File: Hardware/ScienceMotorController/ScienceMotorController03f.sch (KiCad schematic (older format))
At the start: 16 parts

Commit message: changed everything to actuation, added schottky diode, added A/B flags to tiva
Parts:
- added FB?: Ferrite_Bead_Small, symbol Device:Ferrite_Bead_Small
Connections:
- net labels added: +12VA, +3.3VA
- net labels removed: +12V, +3.3V
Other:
- note added: "Sheet 03f: Mixer Output"
- note removed: "Sheet 03f: Motor Driver 6"
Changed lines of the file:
@@
 	7300 4200 7300 4100
 Connection ~ 7300 4100
-$Comp
-L power:+12V #PWR?
-U 1 1 5FACB535
-P 7500 3950
-AR Path="/5F7D111E/5FACB535" Ref="#PWR?"  Part="1"
-AR Path="/5F7D111E/5FA66A7C/5FACB535" Ref="#PWR?"  Part="1"
-F 0 "#PWR?" H 7500 3800 50  0001 C CNN
-F 1 "+12V" H 7515 4123 50  0000 C CNN
-F 2 "" H 7500 3950 50  0001 C CNN
-F 3 "" H 7500 3950 50  0001 C CNN
-	1    7500 3950
-	1    0    0    -1
-$EndComp
 Wire Wire Line
 	7500 3950 7500 4000
@@
 Wire Wire Line
 	5300 4150 5150 4150
-$Comp
-L power:+3.3V #PWR?
-U 1 1 5FACB576
-P 5150 4150
-AR Path="/5F7D111E/5FACB576" Ref="#PWR?"  Part="1"
-AR Path="/5F7D111E/5FA66A7C/5FACB576" Ref="#PWR?"  Part="1"
-F 0 "#PWR?" H 5150 4000 50  0001 C CNN
-F 1 "+3.3V" V 5165 4278 50  0000 L CNN
-F 2 "" H 5150 4150 50  0001 C CNN
-F 3 "" H 5150 4150 50  0001 C CNN
-	1    5150 4150
-	0    -1   -1   0
-$EndComp
-$Comp
-L power:+3.3V #PWR?
-U 1 1 5FACB57C
-P 5150 3850
-AR Path="/5F7D111E/5FACB57C" Ref="#PWR?"  Part="1"
-AR Path="/5F7D111E/5FA66A7C/5FACB57C" Ref="#PWR?"  Part="1"
-F 0 "#PWR?" H 5150 3700 50  0001 C CNN
-F 1 "+3.3V" V 5165 3978 50  0000 L CNN
-F 2 "" H 5150 3850 50  0001 C CNN
-F 3 "" H 5150 3850 50  0001 C CNN
-	1    5150 3850
-	0    -1   -1   0
-$EndComp
 Wire Wire Line
 	5650 3850 5150 3850
@@
 Wire Wire Line
 	5650 3750 5500 3750
-$Comp
-L power:+3.3V #PWR?
-U 1 1 5FACB58A
-P 5150 3750
-AR Path="/5F7D111E/5FACB58A" Ref="#PWR?"  Part="1"
-AR Path="/5F7D111E/5FA66A7C/5FACB58A" Ref="#PWR?"  Part="1"
-F 0 "#PWR?" H 5150 3600 50  0001 C CNN
-F 1 "+3.3V" V 5165 3878 50  0000 L CNN
-F 2 "" H 5150 3750 50  0001 C CNN
-F 3 "" H 5150 3750 50  0001 C CNN
-	1    5150 3750
-	0    -1   -1   0
-$EndComp
 Wire Wire Line
 	5300 3750 5150 3750
@@
 	8100 3600 8200 3600
 Text Notes 7200 6950 0    197  ~ 0
-Sheet 03f: Motor Driver 6
+Sheet 03f: Mixer Output
+$Comp
+L Device:Ferrite_Bead_Small FB?
+U 1 1 5F83E921
+P 8450 4150
+F 0 "FB?" H 8550 4196 50  0000 L CNN
+F 1 "Ferrite_Bead_Small" H 8550 4105 50  0000 L CNN
+F 2 "" V 8380 4150 50  0001 C CNN
+F 3 "~" H 8450 4150 50  0001 C CNN
+	1    8450 4150
+	1    0    0    -1
+$EndComp
+$Comp
+L power:+3.3VA #PWR?
+U 1 1 5F83FF6A
+P 5150 3750
+F 0 "#PWR?" H 5150 3600 50  0001 C CNN
+F 1 "+3.3VA" V 5165 3877 50  0000 L CNN
+F 2 "" H 5150 3750 50  0001 C CNN
+F 3 "" H 5150 3750 50  0001 C CNN
+	1    5150 3750
+	0    -1   -1   0
+$EndComp
+$Comp
+L power:+3.3VA #PWR?
+U 1 1 5F8408BA
+P 5150 3850
+F 0 "#PWR?" H 5150 3700 50  0001 C CNN
+F 1 "+3.3VA" V 5165 3977 50  0000 L CNN
+F 2 "" H 5150 3850 50  0001 C CNN
+F 3 "" H 5150 3850 50  0001 C CNN
+	1    5150 3850
+	0    -1   -1   0
+$EndComp
+$Comp
+L power:+3.3VA #PWR?
+U 1 1 5F840B1F
+P 5150 4150
+F 0 "#PWR?" H 5150 4000 50  0001 C CNN
+F 1 "+3.3VA" V 5165 4277 50  0000 L CNN
+F 2 "" H 5150 4150 50  0001 C CNN
+F 3 "" H 5150 4150 50  0001 C CNN
+	1    5150 4150
+	0    -1   -1   0
+$EndComp
+$Comp
+L power:+12VA #PWR?
+U 1 1 5F8410BA
+P 7500 3950
+F 0 "#PWR?" H 7500 3800 50  0001 C CNN
+F 1 "+12VA" H 7515 4123 50  0000 C CNN
+F 2 "" H 7500 3950 50  0001 C CNN
+F 3 "" H 7500 3950 50  0001 C CNN
+	1    7500 3950
+	1    0    0    -1
+$EndComp
 $EndSCHEMATC

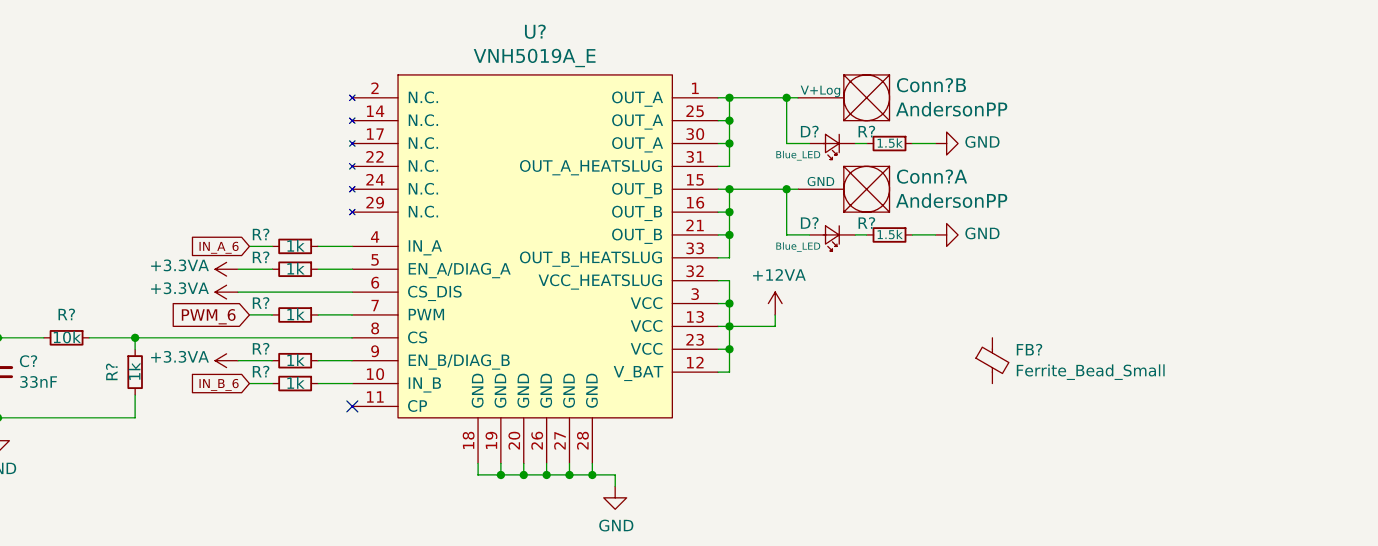
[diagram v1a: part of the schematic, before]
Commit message: added ferrite beads
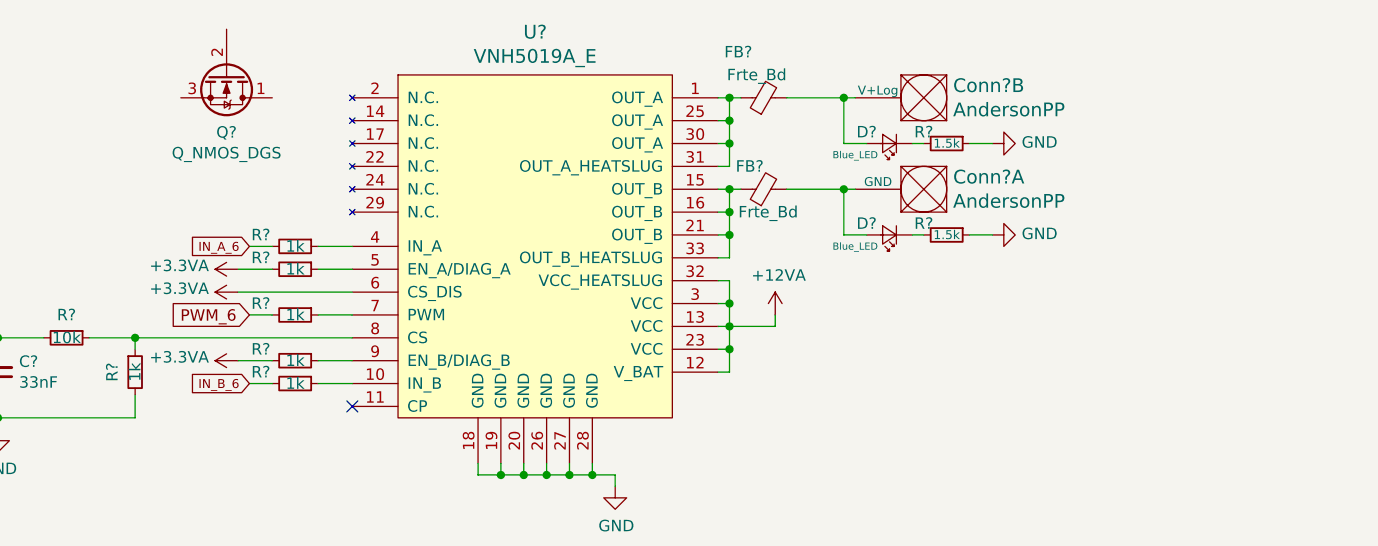
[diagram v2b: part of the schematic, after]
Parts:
- added FB?: Frte_Bd, symbol Device:Ferrite_Bead_Small
- added Q?: Q_NMOS_DGS, symbol Device:Q_NMOS_DGS
- FB?: value Ferrite_Bead_Small -> Frte_Bd
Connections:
- net at FB?.1: now also U?.15 (OUT_B), U?.16 (OUT_B), U?.21 (OUT_B), U?.33 (OUT_B_HEATSLUG)
- net at FB?.2: now also Conn?.1 (GND), D?.2 (A)
- net at U?.1 (OUT_A), U?.25 (OUT_A), U?.30 (OUT_A)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: now also FB?.1; no longer Conn?.2 (V+Log), D?.2 (A)
- new net: Conn?.2 (V+Log), D?.2 (A), FB?.2
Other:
- moved on the sheet: Conn?A, Conn?B, D?, FB?, R?
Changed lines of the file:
@@
 L MRDT_Connectors:AndersonPP Conn?
 U 1 1 5FACB5D5
-P 8000 3300
+P 8250 3300
 AR Path="/5F7D111E/5FACB5D5" Ref="Conn?"  Part="1"
 AR Path="/5F7D111E/5FA66A7C/5FACB5D5" Ref="Conn?"  Part="1"
-F 0 "Conn?" H 7972 3347 60  0000 R CNN
-F 1 "AndersonPP" H 7972 3453 60  0000 R CNN
-F 2 "" H 7850 2750 60  0001 C CNN
-F 3 "" H 7850 2750 60  0001 C CNN
-	1    8000 3300
+F 0 "Conn?" H 8222 3347 60  0000 R CNN
+F 1 "AndersonPP" H 8222 3453 60  0000 R CNN
+F 2 "" H 8100 2750 60  0001 C CNN
+F 3 "" H 8100 2750 60  0001 C CNN
+	1    8250 3300
 	-1   0    0    1
 $EndComp
@@
 L MRDT_Connectors:AndersonPP Conn?
 U 2 1 5FACB5DB
-P 8000 2900
+P 8250 2900
 AR Path="/5F7D111E/5FACB5DB" Ref="Conn?"  Part="2"
 AR Path="/5F7D111E/5FA66A7C/5FACB5DB" Ref="Conn?"  Part="2"
-F 0 "Conn?" H 7972 2947 60  0000 R CNN
-F 1 "AndersonPP" H 7972 3053 60  0000 R CNN
-F 2 "" H 7850 2350 60  0001 C CNN
-F 3 "" H 7850 2350 60  0001 C CNN
-	2    8000 2900
+F 0 "Conn?" H 8222 2947 60  0000 R CNN
+F 1 "AndersonPP" H 8222 3053 60  0000 R CNN
+F 2 "" H 8100 2350 60  0001 C CNN
+F 3 "" H 8100 2350 60  0001 C CNN
+	2    8250 2900
 	-1   0    0    1
 $EndComp
@@
 Connection ~ 4700 4050
 Wire Wire Line
-	7300 3000 7550 3000
-Connection ~ 7300 3000
-Wire Wire Line
-	7300 3400 7550 3400
-Connection ~ 7300 3400
-Wire Wire Line
-	7550 3200 7550 3000
-Connection ~ 7550 3000
-Wire Wire Line
-	7550 3000 7600 3000
-Wire Wire Line
-	7550 3200 7650 3200
-Wire Wire Line
-	7550 3400 7550 3600
-Wire Wire Line
-	7550 3600 7650 3600
-Connection ~ 7550 3400
-Wire Wire Line
-	7550 3400 7600 3400
+	7550 3000 7800 3000
+Wire Wire Line
+	7550 3400 7800 3400
+Wire Wire Line
+	7800 3200 7800 3000
+Connection ~ 7800 3000
+Wire Wire Line
+	7800 3000 7850 3000
+Wire Wire Line
+	7800 3200 7900 3200
+Wire Wire Line
+	7800 3400 7800 3600
+Wire Wire Line
+	7800 3600 7900 3600
+Connection ~ 7800 3400
+Wire Wire Line
+	7800 3400 7850 3400
 $Comp
 L Device:LED_Small D?
 U 1 1 5FACB5EF
-P 7750 3200
+P 8000 3200
 AR Path="/5F7D111E/5FACB5EF" Ref="D?"  Part="1"
 AR Path="/5F7D111E/5FA66A7C/5FACB5EF" Ref="D?"  Part="1"
-F 0 "D?" H 7850 3150 50  0000 C CNN
-F 1 "Blue_LED" H 7900 3250 31  0000 C CNN
-F 2 "" V 7750 3200 50  0001 C CNN
-F 3 "~" V 7750 3200 50  0001 C CNN
-	1    7750 3200
+F 0 "D?" H 8100 3150 50  0000 C CNN
+F 1 "Blue_LED" H 8150 3250 31  0000 C CNN
+F 2 "" V 8000 3200 50  0001 C CNN
+F 3 "~" V 8000 3200 50  0001 C CNN
+	1    8000 3200
 	-1   0    0    1
 $EndComp
@@
 L Device:LED_Small D?
 U 1 1 5FACB5F5
-P 7750 3600
+P 8000 3600
 AR Path="/5F7D111E/5FACB5F5" Ref="D?"  Part="1"
 AR Path="/5F7D111E/5FA66A7C/5FACB5F5" Ref="D?"  Part="1"
-F 0 "D?" H 7850 3550 50  0000 C CNN
-F 1 "Blue_LED" H 7900 3650 31  0000 C CNN
-F 2 "" V 7750 3600 50  0001 C CNN
-F 3 "~" V 7750 3600 50  0001 C CNN
-	1    7750 3600
+F 0 "D?" H 8100 3550 50  0000 C CNN
+F 1 "Blue_LED" H 8150 3650 31  0000 C CNN
+F 2 "" V 8000 3600 50  0001 C CNN
+F 3 "~" V 8000 3600 50  0001 C CNN
+	1    8000 3600
 	-1   0    0    1
 $EndComp
@@
 L Device:R_Small R?
 U 1 1 5FACB5FB
-P 8000 3600
+P 8250 3600
 AR Path="/5F7D111E/5FACB5FB" Ref="R?"  Part="1"
 AR Path="/5F7D111E/5FA66A7C/5FACB5FB" Ref="R?"  Part="1"
-F 0 "R?" V 7950 3500 50  0000 C CNN
-F 1 "1.5k" V 8000 3600 39  0000 C CNN
-F 2 "" H 8000 3600 50  0001 C CNN
-F 3 "~" H 8000 3600 50  0001 C CNN
-	1    8000 3600
+F 0 "R?" V 8200 3500 50  0000 C CNN
+F 1 "1.5k" V 8250 3600 39  0000 C CNN
+F 2 "" H 8250 3600 50  0001 C CNN
+F 3 "~" H 8250 3600 50  0001 C CNN
+	1    8250 3600
 	0    1    1    0
 $EndComp
@@
 L Device:R_Small R?
 U 1 1 5FACB601
-P 8000 3200
+P 8250 3200
 AR Path="/5F7D111E/5FACB601" Ref="R?"  Part="1"
 AR Path="/5F7D111E/5FA66A7C/5FACB601" Ref="R?"  Part="1"
-F 0 "R?" V 7950 3100 50  0000 C CNN
-F 1 "1.5k" V 8000 3200 39  0000 C CNN
-F 2 "" H 8000 3200 50  0001 C CNN
-F 3 "~" H 8000 3200 50  0001 C CNN
-	1    8000 3200
+F 0 "R?" V 8200 3100 50  0000 C CNN
+F 1 "1.5k" V 8250 3200 39  0000 C CNN
+F 2 "" H 8250 3200 50  0001 C CNN
+F 3 "~" H 8250 3200 50  0001 C CNN
+	1    8250 3200
 	0    1    1    0
 $EndComp
 Wire Wire Line
-	7850 3200 7900 3200
-Wire Wire Line
-	7850 3600 7900 3600
+	8100 3200 8150 3200
+Wire Wire Line
+	8100 3600 8150 3600
 $Comp
 L power:GND #PWR?
 U 1 1 5FACB609
-P 8200 3200
+P 8450 3200
 AR Path="/5F7D111E/5FACB609" Ref="#PWR?"  Part="1"
 AR Path="/5F7D111E/5FA66A7C/5FACB609" Ref="#PWR?"  Part="1"
-F 0 "#PWR?" H 8200 2950 50  0001 C CNN
-F 1 "GND" V 8205 3072 50  0000 R CNN
-F 2 "" H 8200 3200 50  0001 C CNN
-F 3 "" H 8200 3200 50  0001 C CNN
-	1    8200 3200
+F 0 "#PWR?" H 8450 2950 50  0001 C CNN
+F 1 "GND" V 8455 3072 50  0000 R CNN
+F 2 "" H 8450 3200 50  0001 C CNN
+F 3 "" H 8450 3200 50  0001 C CNN
+	1    8450 3200
 	0    -1   -1   0
 $EndComp
@@
 L power:GND #PWR?
 U 1 1 5FACB60F
-P 8200 3600
+P 8450 3600
 AR Path="/5F7D111E/5FACB60F" Ref="#PWR?"  Part="1"
 AR Path="/5F7D111E/5FA66A7C/5FACB60F" Ref="#PWR?"  Part="1"
-F 0 "#PWR?" H 8200 3350 50  0001 C CNN
-F 1 "GND" V 8205 3472 50  0000 R CNN
-F 2 "" H 8200 3600 50  0001 C CNN
-F 3 "" H 8200 3600 50  0001 C CNN
-	1    8200 3600
-	0    -1   -1   0
-$EndComp
-Wire Wire Line
-	8100 3200 8200 3200
-Wire Wire Line
-	8100 3600 8200 3600
+F 0 "#PWR?" H 8450 3350 50  0001 C CNN
+F 1 "GND" V 8455 3472 50  0000 R CNN
+F 2 "" H 8450 3600 50  0001 C CNN
+F 3 "" H 8450 3600 50  0001 C CNN
+	1    8450 3600
+	0    -1   -1   0
+$EndComp
+Wire Wire Line
+	8350 3200 8450 3200
+Wire Wire Line
+	8350 3600 8450 3600
 Text Notes 7200 6950 0    197  ~ 0
 Sheet 03f: Mixer Output
@@
 L Device:Ferrite_Bead_Small FB?
 U 1 1 5F83E921
-P 8450 4150
-F 0 "FB?" H 8550 4196 50  0000 L CNN
-F 1 "Ferrite_Bead_Small" H 8550 4105 50  0000 L CNN
-F 2 "" V 8380 4150 50  0001 C CNN
-F 3 "~" H 8450 4150 50  0001 C CNN
-	1    8450 4150
-	1    0    0    -1
+P 7450 3400
+F 0 "FB?" V 7550 3400 50  0000 L CNN
+F 1 "Frte_Bd" V 7350 3250 50  0000 L CNN
+F 2 "" V 7380 3400 50  0001 C CNN
+F 3 "~" H 7450 3400 50  0001 C CNN
+	1    7450 3400
+	0    -1   -1   0
 $EndComp
 $Comp
@@
 	1    0    0    -1
 $EndComp
+$Comp
+L Device:Ferrite_Bead_Small FB?
+U 1 1 5F82955C
+P 7450 3000
+F 0 "FB?" V 7650 3050 50  0000 L CNN
+F 1 "Frte_Bd" V 7550 2900 50  0000 L CNN
+F 2 "" V 7380 3000 50  0001 C CNN
+F 3 "~" H 7450 3000 50  0001 C CNN
+	1    7450 3000
+	0    -1   -1   0
+$EndComp
+Wire Wire Line
+	7350 3000 7300 3000
+Connection ~ 7300 3000
+Wire Wire Line
+	7350 3400 7300 3400
+Connection ~ 7300 3400
+$Comp
+L Device:Q_NMOS_DGS Q?
+U 1 1 5F84285D
+P 5100 2900
+F 0 "Q?" V 5351 2900 50  0000 C CNN
+F 1 "Q_NMOS_DGS" V 5442 2900 50  0000 C CNN
+F 2 "" H 5300 3000 50  0001 C CNN
+F 3 "~" H 5100 2900 50  0001 C CNN
+	1    5100 2900
+	0    1    1    0
+$EndComp
 $EndSCHEMATC

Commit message: schematic review
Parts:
- removed Q?: Q_NMOS_DGS, symbol Device:Q_NMOS_DGS
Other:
- moved on the sheet: Conn?A, Conn?B, D?, FB?, R?

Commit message: fixed hierarchical
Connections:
- net IN_A_6 renamed In_A_6
- net IN_B_6 renamed In_B_6
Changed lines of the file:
@@
 $Descr A4 11693 8268
 encoding utf-8
-Sheet 10 10
+Sheet 9 11
 Title ""
 Date ""
@@
 AR Path="/5F7D111E/5FA66A7C/5FACB523" Ref="U?"  Part="1"
 AR Path="/5F908300/5FACB523" Ref="U?"  Part="1"
+AR Path="/5F7148FA/5FA34ADD/5FACB523" Ref="U?"  Part="1"
 F 0 "U?" H 6450 6087 60  0000 C CNN
 F 1 "VNH5019A_E" H 6450 5981 60  0000 C CNN
@@
 Wire Wire Line
 	7500 4000 7300 4000
-Text GLabel 5200 3950 0    50   Input ~ 0
-PWM_6
 Wire Wire Line
 	5650 3950 5500 3950
@@
 AR Path="/5F7D111E/5FA66A7C/5FACB540" Ref="R?"  Part="1"
 AR Path="/5F908300/5FACB540" Ref="R?"  Part="1"
+AR Path="/5F7148FA/5FA34ADD/5FACB540" Ref="R?"  Part="1"
 F 0 "R?" V 5350 3800 50  0000 C CNN
 F 1 "1k" V 5400 3950 50  0000 C CNN
@@
 AR Path="/5F7D111E/5FA66A7C/5FACB546" Ref="R?"  Part="1"
 AR Path="/5F908300/5FACB546" Ref="R?"  Part="1"
+AR Path="/5F7148FA/5FA34ADD/5FACB546" Ref="R?"  Part="1"
 F 0 "R?" V 4600 4200 50  0000 C CNN
 F 1 "1k" V 4700 4200 50  0000 C CNN
@@
 AR Path="/5F7D111E/5FA66A7C/5FACB54C" Ref="C?"  Part="1"
 AR Path="/5F908300/5FACB54C" Ref="C?"  Part="1"
+AR Path="/5F7148FA/5FA34ADD/5FACB54C" Ref="C?"  Part="1"
 F 0 "C?" H 4008 4154 50  0000 R CNN
 F 1 "33nF" H 4008 4245 50  0000 R CNN
@@
 AR Path="/5F7D111E/5FA66A7C/5FACB552" Ref="D?"  Part="1"
 AR Path="/5F908300/5FACB552" Ref="D?"  Part="1"
+AR Path="/5F7148FA/5FA34ADD/5FACB552" Ref="D?"  Part="1"
 F 0 "D?" V 3900 4050 50  0000 R CNN
 F 1 "D_Zener_Small" V 3800 4100 50  0000 R CNN
@@
 AR Path="/5F7D111E/5FA66A7C/5FACB558" Ref="R?"  Part="1"
 AR Path="/5F908300/5FACB558" Ref="R?"  Part="1"
+AR Path="/5F7148FA/5FA34ADD/5FACB558" Ref="R?"  Part="1"
 F 0 "R?" V 4300 4050 50  0000 C CNN
 F 1 "10k" V 4400 4050 50  0000 C CNN
@@
 	3850 4050 3650 4050
 Connection ~ 3850 4050
-Text GLabel 3650 4050 0    39   Output ~ 0
-Current_Sense_6
 $Comp
 L Device:R_Small R?
@@
 AR Path="/5F7D111E/5FA66A7C/5FACB56E" Ref="R?"  Part="1"
 AR Path="/5F908300/5FACB56E" Ref="R?"  Part="1"
+AR Path="/5F7148FA/5FA34ADD/5FACB56E" Ref="R?"  Part="1"
 F 0 "R?" V 5350 4000 50  0000 C CNN
 F 1 "1k" V 5400 4150 50  0000 C CNN
@@
 AR Path="/5F7D111E/5FA66A7C/5FACB583" Ref="R?"  Part="1"
 AR Path="/5F908300/5FACB583" Ref="R?"  Part="1"
+AR Path="/5F7148FA/5FA34ADD/5FACB583" Ref="R?"  Part="1"
 F 0 "R?" V 5350 3600 50  0000 C CNN
 F 1 "1k" V 5400 3750 50  0000 C CNN
@@
 AR Path="/5F7D111E/5FA66A7C/5FACB591" Ref="R?"  Part="1"
 AR Path="/5F908300/5FACB591" Ref="R?"  Part="1"
+AR Path="/5F7148FA/5FA34ADD/5FACB591" Ref="R?"  Part="1"
 F 0 "R?" V 5350 3500 50  0000 C CNN
 F 1 "1k" V 5400 3650 50  0000 C CNN
@@
 Wire Wire Line
 	5650 3650 5500 3650
-Text GLabel 5200 3650 0    39   Input ~ 0
-IN_A_6
 Wire Wire Line
 	5200 3650 5300 3650
-Text GLabel 5200 4250 0    39   Input ~ 0
-IN_B_6
 $Comp
 L Device:R_Small R?
@@
 AR Path="/5F7D111E/5FA66A7C/5FACB59B" Ref="R?"  Part="1"
 AR Path="/5F908300/5FACB59B" Ref="R?"  Part="1"
+AR Path="/5F7148FA/5FA34ADD/5FACB59B" Ref="R?"  Part="1"
 F 0 "R?" V 5350 4100 50  0000 C CNN
 F 1 "1k" V 5400 4250 50  0000 C CNN
@@
 AR Path="/5F7D111E/5FA66A7C/5FACB5B3" Ref="#PWR?"  Part="1"
 AR Path="/5F908300/5FACB5B3" Ref="#PWR?"  Part="1"
+AR Path="/5F7148FA/5FA34ADD/5FACB5B3" Ref="#PWR?"  Part="1"
 F 0 "#PWR?" H 6800 4450 50  0001 C CNN
 F 1 "GND" H 6805 4527 50  0000 C CNN
@@
 AR Path="/5F7D111E/5FA66A7C/5FACB5BD" Ref="#PWR?"  Part="1"
 AR Path="/5F908300/5FACB5BD" Ref="#PWR?"  Part="1"
+AR Path="/5F7148FA/5FA34ADD/5FACB5BD" Ref="#PWR?"  Part="1"
 F 0 "#PWR?" H 4100 4200 50  0001 C CNN
 F 1 "GND" H 4105 4277 50  0000 C CNN
@@
 AR Path="/5F7D111E/5FA66A7C/5FACB5D5" Ref="Conn?"  Part="1"
 AR Path="/5F908300/5FACB5D5" Ref="Conn?"  Part="1"
+AR Path="/5F7148FA/5FA34ADD/5FACB5D5" Ref="Conn?"  Part="1"
 F 0 "Conn?" H 8522 3347 60  0000 R CNN
 F 1 "AndersonPP" H 8522 3453 60  0000 R CNN
@@
 AR Path="/5F7D111E/5FA66A7C/5FACB5DB" Ref="Conn?"  Part="2"
 AR Path="/5F908300/5FACB5DB" Ref="Conn?"  Part="2"
+AR Path="/5F7148FA/5FA34ADD/5FACB5DB" Ref="Conn?"  Part="2"
 F 0 "Conn?" H 8522 2947 60  0000 R CNN
 F 1 "AndersonPP" H 8522 3053 60  0000 R CNN
@@
 AR Path="/5F7D111E/5FA66A7C/5FACB5EF" Ref="D?"  Part="1"
 AR Path="/5F908300/5FACB5EF" Ref="D?"  Part="1"
+AR Path="/5F7148FA/5FA34ADD/5FACB5EF" Ref="D?"  Part="1"
 F 0 "D?" H 8400 3150 50  0000 C CNN
 F 1 "Blue_LED" H 8450 3250 31  0000 C CNN
@@
 AR Path="/5F7D111E/5FA66A7C/5FACB5F5" Ref="D?"  Part="1"
 AR Path="/5F908300/5FACB5F5" Ref="D?"  Part="1"
+AR Path="/5F7148FA/5FA34ADD/5FACB5F5" Ref="D?"  Part="1"
 F 0 "D?" H 8400 3550 50  0000 C CNN
 F 1 "Blue_LED" H 8450 3650 31  0000 C CNN
@@
 AR Path="/5F7D111E/5FA66A7C/5FACB5FB" Ref="R?"  Part="1"
 AR Path="/5F908300/5FACB5FB" Ref="R?"  Part="1"
+AR Path="/5F7148FA/5FA34ADD/5FACB5FB" Ref="R?"  Part="1"
 F 0 "R?" V 8500 3500 50  0000 C CNN
 F 1 "1.5k" V 8550 3600 39  0000 C CNN
@@
 AR Path="/5F7D111E/5FA66A7C/5FACB601" Ref="R?"  Part="1"
 AR Path="/5F908300/5FACB601" Ref="R?"  Part="1"
+AR Path="/5F7148FA/5FA34ADD/5FACB601" Ref="R?"  Part="1"
 F 0 "R?" V 8500 3100 50  0000 C CNN
 F 1 "1.5k" V 8550 3200 39  0000 C CNN
@@
 AR Path="/5F7D111E/5FA66A7C/5FACB609" Ref="#PWR?"  Part="1"
 AR Path="/5F908300/5FACB609" Ref="#PWR?"  Part="1"
+AR Path="/5F7148FA/5FA34ADD/5FACB609" Ref="#PWR?"  Part="1"
 F 0 "#PWR?" H 8750 2950 50  0001 C CNN
 F 1 "GND" V 8755 3072 50  0000 R CNN
@@
 AR Path="/5F7D111E/5FA66A7C/5FACB60F" Ref="#PWR?"  Part="1"
 AR Path="/5F908300/5FACB60F" Ref="#PWR?"  Part="1"
+AR Path="/5F7148FA/5FA34ADD/5FACB60F" Ref="#PWR?"  Part="1"
 F 0 "#PWR?" H 8750 3350 50  0001 C CNN
 F 1 "GND" V 8755 3472 50  0000 R CNN
@@
 AR Path="/5F7D111E/5FA66A7C/5F83E921" Ref="FB?"  Part="1"
 AR Path="/5F908300/5F83E921" Ref="FB?"  Part="1"
+AR Path="/5F7148FA/5FA34ADD/5F83E921" Ref="FB?"  Part="1"
 F 0 "FB?" V 7850 3400 50  0000 L CNN
 F 1 "Frte_Bd" V 7650 3250 50  0000 L CNN
@@
 AR Path="/5F7D111E/5FA66A7C/5F83FF6A" Ref="#PWR?"  Part="1"
 AR Path="/5F908300/5F83FF6A" Ref="#PWR?"  Part="1"
+AR Path="/5F7148FA/5FA34ADD/5F83FF6A" Ref="#PWR?"  Part="1"
 F 0 "#PWR?" H 5150 3600 50  0001 C CNN
 F 1 "+3.3VA" V 5165 3877 50  0000 L CNN
@@
 AR Path="/5F7D111E/5FA66A7C/5F8408BA" Ref="#PWR?"  Part="1"
 AR Path="/5F908300/5F8408BA" Ref="#PWR?"  Part="1"
+AR Path="/5F7148FA/5FA34ADD/5F8408BA" Ref="#PWR?"  Part="1"
 F 0 "#PWR?" H 5150 3700 50  0001 C CNN
 F 1 "+3.3VA" V 5165 3977 50  0000 L CNN
@@
 AR Path="/5F7D111E/5FA66A7C/5F840B1F" Ref="#PWR?"  Part="1"
 AR Path="/5F908300/5F840B1F" Ref="#PWR?"  Part="1"
+AR Path="/5F7148FA/5FA34ADD/5F840B1F" Ref="#PWR?"  Part="1"
 F 0 "#PWR?" H 5150 4000 50  0001 C CNN
 F 1 "+3.3VA" V 5165 4277 50  0000 L CNN
@@
 AR Path="/5F7D111E/5FA66A7C/5F8410BA" Ref="#PWR?"  Part="1"
 AR Path="/5F908300/5F8410BA" Ref="#PWR?"  Part="1"
+AR Path="/5F7148FA/5FA34ADD/5F8410BA" Ref="#PWR?"  Part="1"
 F 0 "#PWR?" H 7500 3800 50  0001 C CNN
 F 1 "+12VA" H 7515 4123 50  0000 C CNN
@@
 AR Path="/5F7D111E/5FA66A7C/5F82955C" Ref="FB?"  Part="1"
 AR Path="/5F908300/5F82955C" Ref="FB?"  Part="1"
+AR Path="/5F7148FA/5FA34ADD/5F82955C" Ref="FB?"  Part="1"
 F 0 "FB?" V 7950 3050 50  0000 L CNN
 F 1 "Frte_Bd" V 7850 2900 50  0000 L CNN
@@
 Wire Wire Line
 	7300 3400 7650 3400
+Text HLabel 5200 3650 0    50   Input ~ 0
+In_A_6
+Text HLabel 5200 4250 0    50   Input ~ 0
+In_B_6
+Text HLabel 5200 3950 0    50   Input ~ 0
+PWM_6
+Text HLabel 3650 4050 0    50   Output ~ 0
+Current_Sense_6
 $EndSCHEMATC
